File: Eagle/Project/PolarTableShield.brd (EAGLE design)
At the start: 56 x 59.7 mm, 47 parts, among them IC2 LM358D, J1 Pi Power Jack, J10 LED + Radio, J2 Header - Right angled, female, J3 Pi Connection, J5 IR Sensors, J6 Switch A + B, J7 Switch C + D, J8 Switch E + F, Q1 BC337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

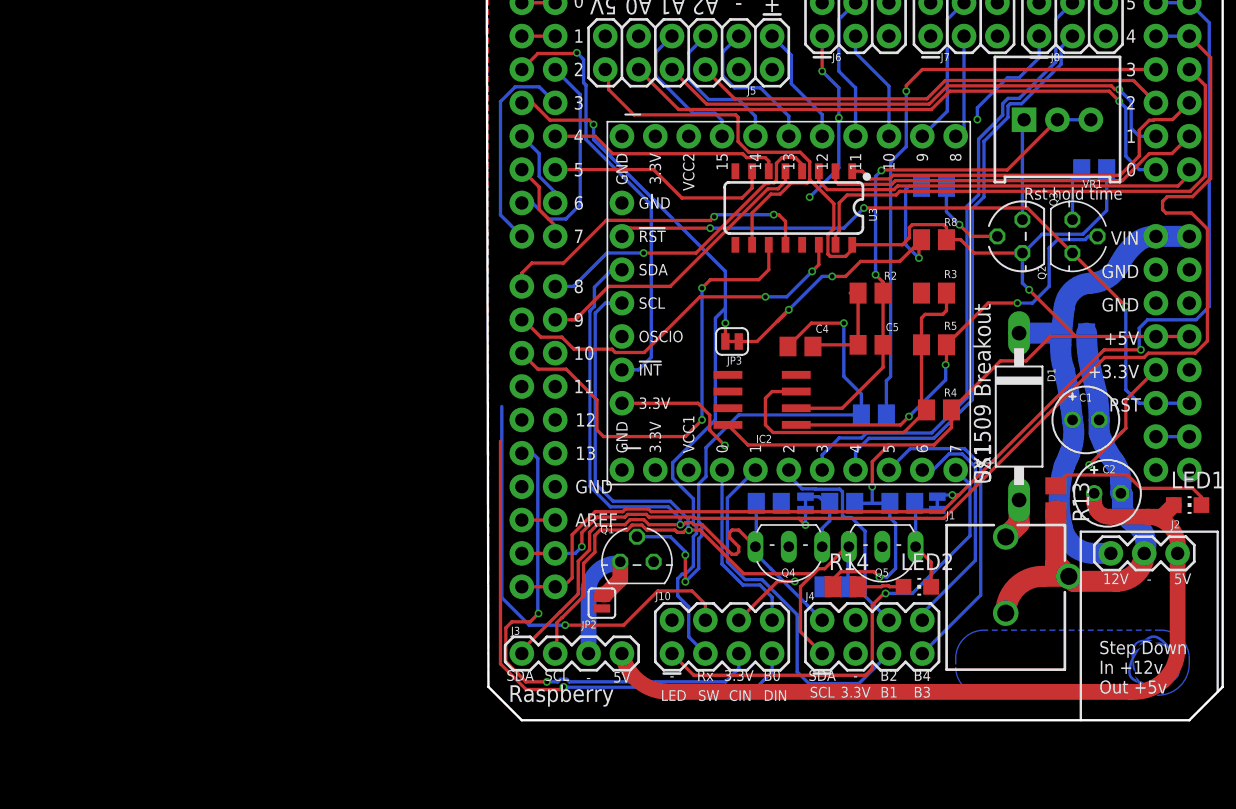
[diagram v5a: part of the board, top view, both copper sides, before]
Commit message: Added a LED for error signals
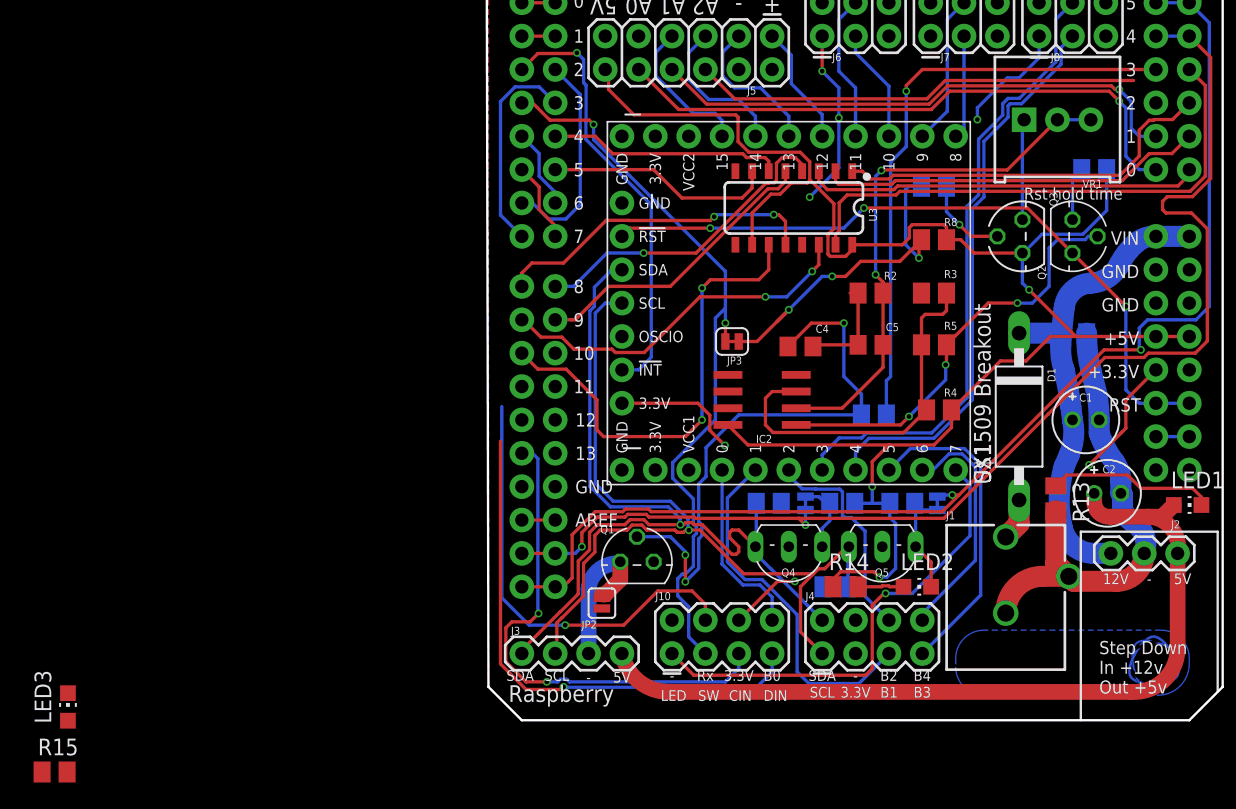
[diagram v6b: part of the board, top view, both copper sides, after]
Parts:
- added LED3: (no value), led:CHIP-LED0805
- added R15: 1k, rcl:M0805
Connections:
- new net ERROR: B1.A2, R15.2
- new net N$11: LED3.A, R15.1
- net A2: no longer B1.A2
- net GND: now also LED3.C
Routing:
- net A2: track 36.5 -> 34.1 mm
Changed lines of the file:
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@@
 <attribute name="VALUE" x="25.908" y="7.62" size="1.27" layer="27"/>
+</element>
+<element name="LED3" library="led" library_urn="urn:adsk.eagle:library:259" package="CHIP-LED0805" package3d_urn="urn:adsk.eagle:package:15818/2" value="" x="-32.004" y="1.016">
+<attribute name="NAME" x="-33.274" y="-0.254" size="1.27" layer="25" rot="R90"/>
+<attribute name="VALUE" x="-29.464" y="-0.254" size="1.27" layer="27" rot="R90"/>
+</element>
+<element name="R15" library="rcl" library_urn="urn:adsk.eagle:library:334" package="M0805" package3d_urn="urn:adsk.eagle:package:23556/1" value="1k" x="-33.02" y="-3.937">
+<attribute name="NAME" x="-34.29" y="-2.667" size="1.27" layer="25"/>
+<attribute name="SPICEPREFIX" value="R" x="-33.02" y="-3.937" size="1.778" layer="27" display="off"/>
+<attribute name="VALUE" x="-34.29" y="-6.477" size="1.27" layer="27"/>
 </element>
 </elements>
@@
 <wire x1="37.211" y1="46.609" x2="39.497" y2="48.895" width="0.254" layer="16"/>
 <wire x1="39.497" y1="48.895" x2="40.386" y2="48.895" width="0.254" layer="16"/>
+<contactref element="LED3" pad="C"/>
+<wire x1="41.91" y1="52.07" x2="41.91" y2="54.61" width="0" layer="19" extent="1-1"/>
+<wire x1="33.655" y1="52.07" x2="37.211" y2="46.609" width="0" layer="19" extent="16-16"/>
+<wire x1="33.655" y1="54.61" x2="33.655" y2="52.07" width="0" layer="19" extent="1-1"/>
+<wire x1="26.67" y1="48.133" x2="33.655" y2="52.07" width="0" layer="19" extent="16-16"/>
+<wire x1="25.4" y1="54.61" x2="25.4" y2="52.07" width="0" layer="19" extent="1-1"/>
+<wire x1="23.876" y1="36.189" x2="24.4475" y2="39.8145" width="0" layer="19" extent="1-16"/>
+<wire x1="27.52786875" y1="32.512" x2="23.876" y2="36.189" width="0" layer="19" extent="1-1"/>
+<wire x1="23.428" y1="26.289" x2="24.699" y2="28.448" width="0" layer="19" extent="1-1"/>
+<wire x1="32.959" y1="32.512" x2="28.133" y2="32.512" width="0" layer="19" extent="1-1"/>
+<wire x1="18.796" y1="41.789" x2="24.4475" y2="39.8145" width="0" layer="19" extent="1-16"/>
+<wire x1="19.05" y1="49.53" x2="25.4" y2="49.403" width="0" layer="19" extent="1-1"/>
+<wire x1="11.43" y1="52.07" x2="19.05" y2="49.53" width="0" layer="19" extent="1-1"/>
+<wire x1="10.16" y1="39.37" x2="18.796" y2="41.789" width="0" layer="19" extent="1-1"/>
+<wire x1="50.8" y1="34.29" x2="37.211" y2="45.72" width="0" layer="19" extent="1-1"/>
+<wire x1="53.34" y1="34.29" x2="50.8" y2="34.29" width="0" layer="19" extent="1-1"/>
+<wire x1="53.34" y1="31.75" x2="53.34" y2="34.29" width="0" layer="19" extent="1-1"/>
+<wire x1="50.8" y1="31.75" x2="50.8" y2="34.29" width="0" layer="19" extent="1-1"/>
+<wire x1="12.573" y1="12.065" x2="23.428" y2="26.289" width="0" layer="19" extent="1-1"/>
+<wire x1="13.97" y1="7.62" x2="12.573" y2="12.065" width="0" layer="19" extent="1-1"/>
+<wire x1="8.636" y1="8.509" x2="12.573" y2="12.065" width="0" layer="19" extent="1-1"/>
+<wire x1="5.08" y1="17.78" x2="12.573" y2="12.065" width="0" layer="19" extent="1-1"/>
+<wire x1="2.54" y1="17.78" x2="5.08" y2="17.78" width="0" layer="19" extent="1-1"/>
+<wire x1="27.94" y1="7.62" x2="13.97" y2="7.62" width="0" layer="19" extent="1-1"/>
+<wire x1="-32.004" y1="2.066" x2="2.54" y2="17.78" width="0" layer="19" extent="1-1"/>
 </signal>
 <signal name="3.3V" class="3">
@@
 </signal>
 <signal name="A2" class="4">
-<contactref element="B1" pad="A2"/>
 <contactref element="J5" pad="6"/>
-<wire x1="50.8" y1="46.99" x2="49.0982" y2="48.6918" width="0.254" layer="1"/>
 <wire x1="49.0982" y1="48.6918" x2="34.766125" y2="48.6918" width="0.254" layer="1"/>
 <wire x1="34.766125" y1="48.6918" x2="33.371925" y2="47.2976" width="0.254" layer="1"/>
@@
 <wire x1="0.9144" y1="21.2344" x2="2.54" y2="25.4" width="0" layer="19" extent="1-1"/>
 </signal>
+<signal name="ERROR">
+<contactref element="B1" pad="A2"/>
+<contactref element="R15" pad="2"/>
+<wire x1="-32.07" y1="-3.937" x2="50.8" y2="46.99" width="0" layer="19" extent="1-1"/>
+</signal>
+<signal name="N$11">
+<contactref element="R15" pad="1"/>
+<contactref element="LED3" pad="A"/>
+<wire x1="-32.004" y1="-0.034" x2="-33.97" y2="-3.937" width="0" layer="19" extent="1-1"/>
+</signal>
 </signals>

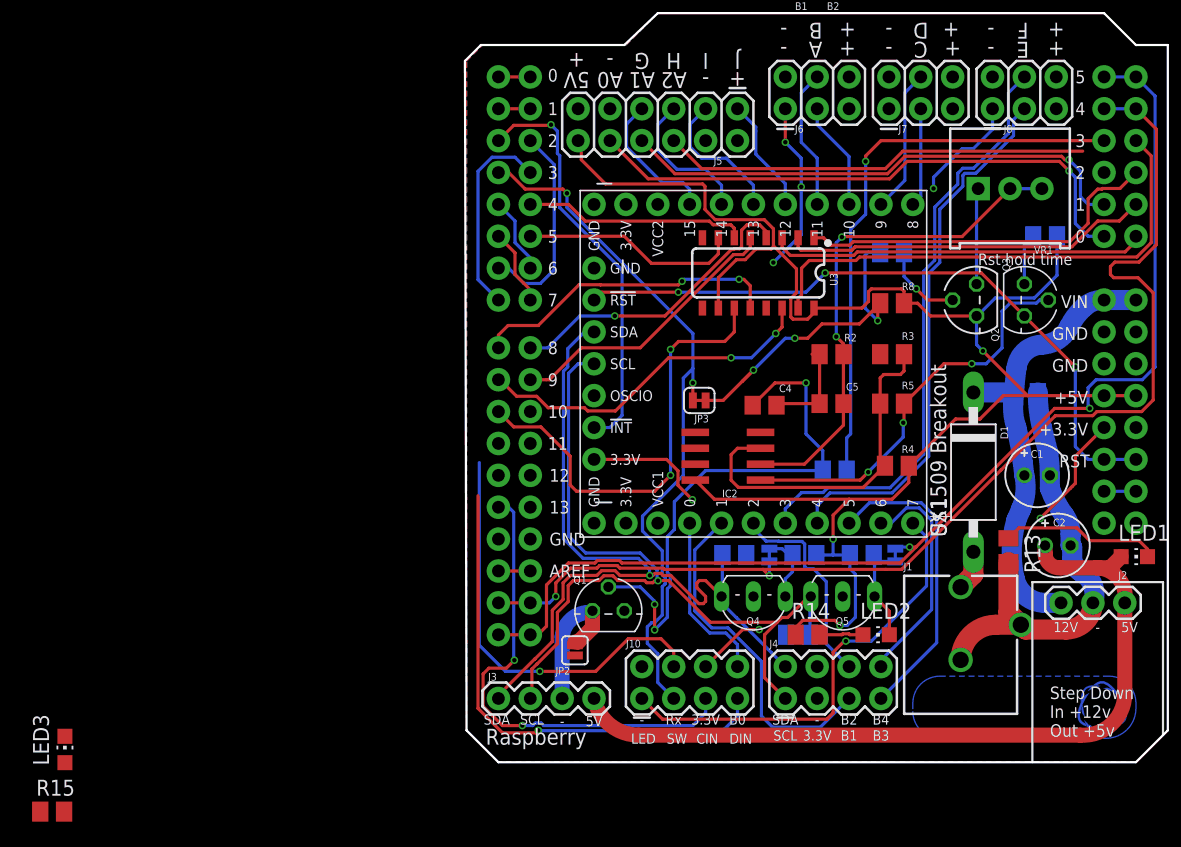
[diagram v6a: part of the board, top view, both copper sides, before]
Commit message: Moved the relative encode switches to the Arduino
Added hardware XOR on the relative encode switches.
Combined the main switch and encoder interrupt connections.
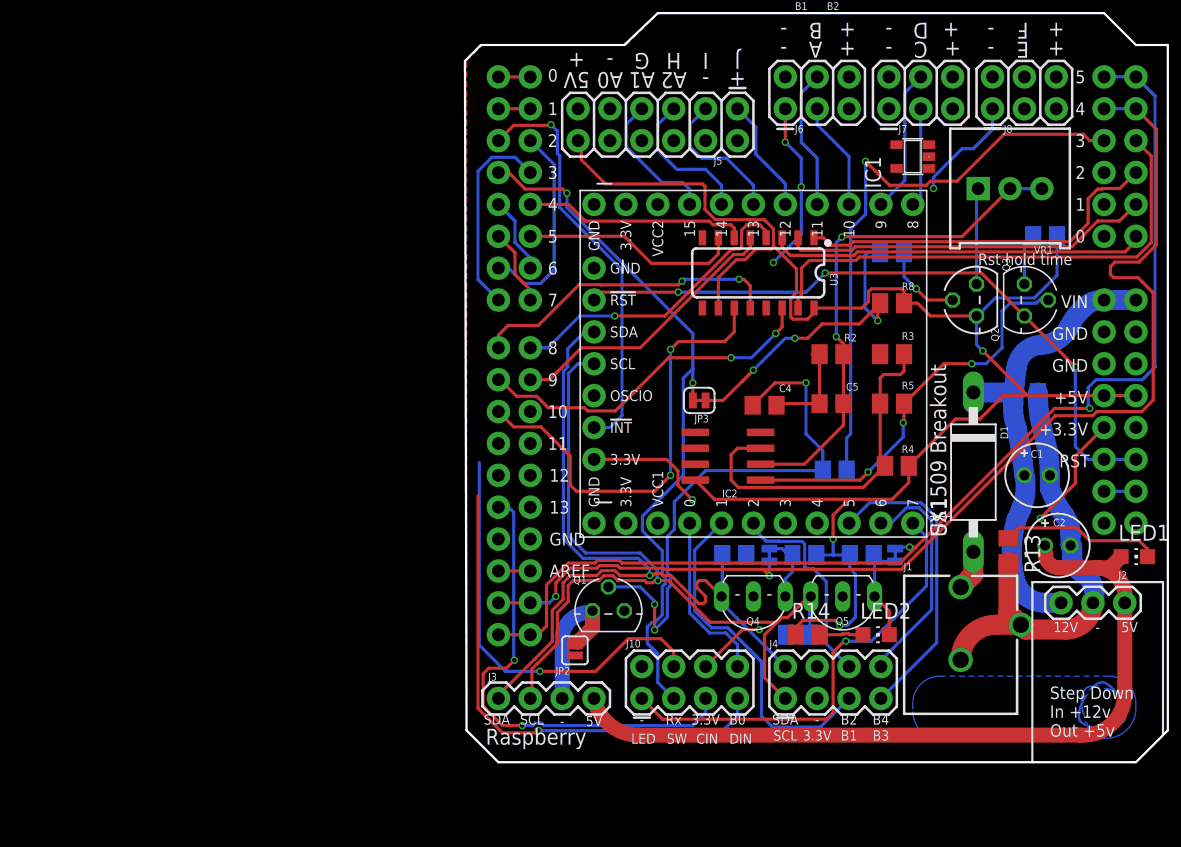
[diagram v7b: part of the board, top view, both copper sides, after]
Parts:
- removed LED3: (no value), led:CHIP-LED0805
- removed R15: 1k, rcl:M0805
- added IC1: 74AHC1G86DBV, 74xx-little-us:SOT23-5
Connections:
- removed net A0: B1.A0, J5.10
- removed net A1: B1.A1, J5.8
- removed net D3_WAKE_SW: B1.D3, J10.3, JP3.1
- removed net ERROR: B1.A2, R15.2
- removed net N$11: LED3.A, R15.1
- removed net SW_E: J8.3, U$1.O4
- removed net SW_F: J8.4, U$1.O3
- new net A0_SW_E: B1.A0, IC1.1, J8.3
- new net A1_SW_F: B1.A1, IC1.2, J8.4
- new net A2_WAKE_SW: B1.A2, B1.D3, IC1.4, J10.3, JP3.1
- new net B5: J4.7, U$1.O5
- new net B6: J4.8, U$1.O6
- new net VCC: IC1.5
- net B3: now also J5.8, U$1.O3; no longer J4.7, U$1.O5
- net B4: now also J5.10, U$1.O4; no longer J4.8, U$1.O6
- net GND: now also IC1.3; no longer LED3.C
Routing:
- net D3_WAKE_SW: track 57.1 -> 0.00 mm, vias 2 -> 0
- net A2_WAKE_SW: track 0.00 -> 56.3 mm, vias 0 -> 2
- net SW_F: track 47.9 -> 0.00 mm
- net A0: track 45.8 -> 0.00 mm, vias 1 -> 0
- net SW_E: track 43.3 -> 0.00 mm
- net A1: track 41.3 -> 0.00 mm, vias 1 -> 0
- net A2: track 34.1 -> 0.00 mm
- net B5: track 0.00 -> 24.4 mm
- net B3: track 24.4 -> 0.00 mm
- net B6: track 0.00 -> 18.3 mm
- net B4: track 18.3 -> 0.00 mm
- net PIPOWER_SIGNAL: track 45.2 -> 46.9 mm
